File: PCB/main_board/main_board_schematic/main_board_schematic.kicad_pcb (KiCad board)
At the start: 2 copper layers, 257 parts, among them J1 Conn_01x02, J2 Conn_01x02, J3 Conn_01x02, P1 USB_C_Plug_USB2.0, SW1 SW_MEC_5G, SW10 SW_MEC_5G, SW100 SW_MEC_5G, SW101 SW_MEC_5G, SW102 SW_MEC_5G, SW103 SW_MEC_5G, SW104 SW_MEC_5G, SW105 SW_MEC_5G, SW106 SW_MEC_5G, SW107 SW_MEC_5G, SW108 SW_MEC_5G, SW11 SW_MEC_5G, SW12 SW_MEC_5G, SW13 SW_MEC_5G, SW14 SW_MEC_5G, SW15 SW_MEC_5G, SW16 SW_MEC_5G, SW17 SW_MEC_5G, SW18 SW_MEC_5G, SW19 SW_MEC_5G, SW2 SW_MEC_5G, SW20 SW_MEC_5G, SW21 SW_MEC_5G, SW22 SW_MEC_5G, SW23 SW_MEC_5G, SW24 SW_MEC_5G, SW25 SW_MEC_5G, SW26 SW_MEC_5G, SW27 SW_MEC_5G, SW28 SW_MEC_5G, SW29 SW_MEC_5G, SW3 SW_MEC_5G, SW30 SW_MEC_5G, SW31 SW_MEC_5G, SW32 SW_MEC_5G, SW33 SW_MEC_5G, SW34 SW_MEC_5G, SW35 SW_MEC_5G, SW36 SW_MEC_5G, SW37 SW_MEC_5G, SW38 SW_MEC_5G, SW39 SW_MEC_5G, SW4 SW_MEC_5G, SW40 SW_MEC_5G, SW41 SW_MEC_5G, SW42 SW_MEC_5G, SW43 SW_MEC_5G, SW44 SW_MEC_5G, SW45 SW_MEC_5G, SW46 SW_MEC_5G, SW47 SW_MEC_5G, SW48 SW_MEC_5G, SW49 SW_MEC_5G, SW5 SW_MEC_5G, SW50 SW_MEC_5G, SW51 SW_MEC_5G, SW52 SW_MEC_5G, SW53 SW_MEC_5G, SW54 SW_MEC_5G, SW55 SW_MEC_5G, SW56 SW_MEC_5G, SW57 SW_MEC_5G, SW58 SW_MEC_5G, SW59 SW_MEC_5G, SW6 SW_MEC_5G, SW60 SW_MEC_5G, SW61 SW_MEC_5G, SW62 SW_MEC_5G, SW63 SW_MEC_5G, SW64 SW_MEC_5G, SW65 SW_MEC_5G, SW66 SW_MEC_5G, SW67 SW_MEC_5G, SW68 SW_MEC_5G, SW69 SW_MEC_5G, SW7 SW_MEC_5G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

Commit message: Placed large portion of the diodes
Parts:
- removed SW1, SW10, SW104, SW105, SW106, SW108, SW11, SW12, SW13, SW14, SW15, SW16, SW17, SW18, SW19, SW2, SW21, SW22, SW23, SW24, SW25, SW26, SW27, SW28, SW29, SW3, SW31, SW32, SW33, SW34, SW35, SW36, SW37, SW38, SW39, SW4, SW41, SW42, SW43, SW44, SW45, SW46, SW47, SW48, SW49, SW5, SW55, SW56, SW57, SW58, SW59, SW6, SW60, SW61, SW62, SW63, SW64, SW65, SW66, SW67, SW68, SW7, SW70, SW71, SW72, SW73, SW74, SW75, SW76, SW77, SW78, SW79, SW8, SW81, SW82, SW83, SW84, SW85, SW86, SW88, SW89, SW9, SW91, SW92, SW93, SW94, SW96, SW97, SW98, SW99: SW_MEC_5G, Button_Switch_Keyboard:SW_Cherry_MX_1.00u_PCB
- removed SW100, SW87: SW_MEC_5G, Button_Switch_Keyboard:SW_Cherry_MX_2.00u_Vertical_PCB
- removed SW101, SW102, SW103, SW50, SW51, SW52, SW54: SW_MEC_5G, Button_Switch_Keyboard:SW_Cherry_MX_1.25u_PCB
- removed SW107, SW69: SW_MEC_5G, Button_Switch_Keyboard:SW_Cherry_MX_2.00u_PCB
- removed SW20, SW80: SW_MEC_5G, Button_Switch_Keyboard:SW_Cherry_MX_1.50u_PCB
- removed SW30: SW_MEC_5G, Button_Switch_Keyboard:SW_Cherry_MX_1.75u_PCB
- removed SW40, SW90: SW_MEC_5G, Button_Switch_Keyboard:SW_Cherry_MX_2.25u_PCB
- removed SW53: SW_MEC_5G, Button_Switch_Keyboard:SW_Cherry_MX_6.25u_PCB
- removed SW95: SW_MEC_5G, Button_Switch_Keyboard:SW_Cherry_MX_2.75u_PCB
- added MX1: MX_SW_solder, PCM_marbastlib-mx:SW_MX_1u, F.Cu at (28.9, 28.6)
- added MX10: MX_SW_solder, PCM_marbastlib-mx:SW_MX_1u, F.Cu at (28.9, 52.4)
- added MX100: MX_SW_solder, PCM_marbastlib-mx:SW_MX_1u, F.Cu at (438.5, 119.1)
- added MX101: MX_SW_solder, PCM_marbastlib-mx:SW_MX_1.25u, F.Cu at (245.6, 128.6)
- added MX102: MX_SW_solder, PCM_marbastlib-mx:SW_MX_1.25u, F.Cu at (269.4, 128.6)
- added MX103: MX_SW_solder, PCM_marbastlib-mx:SW_MX_1.25u, F.Cu at (293.2, 128.6)
- added MX104: MX_SW_solder, PCM_marbastlib-mx:SW_MX_1u, F.Cu at (319.4, 128.6)
- added MX105: MX_SW_solder, PCM_marbastlib-mx:SW_MX_1u, F.Cu at (338.5, 128.6)
- added MX106: MX_SW_solder, PCM_marbastlib-mx:SW_MX_1u, F.Cu at (357.5, 128.6)
- added MX107: MX_SW_solder, PCM_marbastlib-mx:SW_MX_1u, F.Cu at (390.8, 128.6)
- added MX108: MX_SW_solder, PCM_marbastlib-mx:SW_MX_1u, F.Cu at (419.4, 128.6)
- added MX11: MX_SW_solder, PCM_marbastlib-mx:SW_MX_1u, F.Cu at (47.9, 52.4)
- added MX12: MX_SW_solder, PCM_marbastlib-mx:SW_MX_1u, F.Cu at (67.0, 52.4)
- added MX13: MX_SW_solder, PCM_marbastlib-mx:SW_MX_1u, F.Cu at (86.0, 52.4)
- added MX14: MX_SW_solder, PCM_marbastlib-mx:SW_MX_1u, F.Cu at (105.1, 52.4)
- added MX15: MX_SW_solder, PCM_marbastlib-mx:SW_MX_1u, F.Cu at (124.1, 52.4)
- added MX16: MX_SW_solder, PCM_marbastlib-mx:SW_MX_1u, F.Cu at (143.2, 52.4)
- added MX17: MX_SW_solder, PCM_marbastlib-mx:SW_MX_1u, F.Cu at (162.2, 52.4)
- added MX18: MX_SW_solder, PCM_marbastlib-mx:SW_MX_1u, F.Cu at (181.3, 52.4)
- added MX19: MX_SW_solder, PCM_marbastlib-mx:SW_MX_1u, F.Cu at (200.3, 52.4)
- added MX2: MX_SW_solder, PCM_marbastlib-mx:SW_MX_1u, F.Cu at (67.0, 28.6)
- added MX20: MX_SW_solder, PCM_marbastlib-mx:SW_MX_1.5u, F.Cu at (33.7, 71.4)
- added MX21: MX_SW_solder, PCM_marbastlib-mx:SW_MX_1u, F.Cu at (57.5, 71.4)
- added MX22: MX_SW_solder, PCM_marbastlib-mx:SW_MX_1u, F.Cu at (76.5, 71.4)
- added MX23: MX_SW_solder, PCM_marbastlib-mx:SW_MX_1u, F.Cu at (95.6, 71.4)
- added MX24: MX_SW_solder, PCM_marbastlib-mx:SW_MX_1u, F.Cu at (114.6, 71.4)
- added MX25: MX_SW_solder, PCM_marbastlib-mx:SW_MX_1u, F.Cu at (133.7, 71.4)
- added MX26: MX_SW_solder, PCM_marbastlib-mx:SW_MX_1u, F.Cu at (152.7, 71.4)
- added MX27: MX_SW_solder, PCM_marbastlib-mx:SW_MX_1u, F.Cu at (171.8, 71.4)
- added MX28: MX_SW_solder, PCM_marbastlib-mx:SW_MX_1u, F.Cu at (190.8, 71.4)
- added MX29: MX_SW_solder, PCM_marbastlib-mx:SW_MX_1u, F.Cu at (209.9, 71.4)
- added MX3: MX_SW_solder, PCM_marbastlib-mx:SW_MX_1u, F.Cu at (86.0, 28.6)
- added MX30: MX_SW_solder, PCM_marbastlib-mx:SW_MX_1.75u, F.Cu at (36.0, 90.5)
- added MX31: MX_SW_solder, PCM_marbastlib-mx:SW_MX_1u, F.Cu at (62.2, 90.5)
- added MX32: MX_SW_solder, PCM_marbastlib-mx:SW_MX_1u, F.Cu at (81.3, 90.5)
- added MX33: MX_SW_solder, PCM_marbastlib-mx:SW_MX_1u, F.Cu at (100.3, 90.5)
- added MX34: MX_SW_solder, PCM_marbastlib-mx:SW_MX_1u, F.Cu at (119.4, 90.5)
- added MX35: MX_SW_solder, PCM_marbastlib-mx:SW_MX_1u, F.Cu at (138.4, 90.5)
- added MX36: MX_SW_solder, PCM_marbastlib-mx:SW_MX_1u, F.Cu at (157.5, 90.5)
- added MX37: MX_SW_solder, PCM_marbastlib-mx:SW_MX_1u, F.Cu at (176.5, 90.5)
- added MX38: MX_SW_solder, PCM_marbastlib-mx:SW_MX_1u, F.Cu at (195.6, 90.5)
- added MX39: MX_SW_solder, PCM_marbastlib-mx:SW_MX_1u, F.Cu at (214.6, 90.5)
- added MX4: MX_SW_solder, PCM_marbastlib-mx:SW_MX_1u, F.Cu at (105.1, 28.6)
- added MX40: MX_SW_solder, PCM_marbastlib-mx:SW_MX_1u, F.Cu at (40.8, 109.5)
- added MX41: MX_SW_solder, PCM_marbastlib-mx:SW_MX_1u, F.Cu at (71.8, 109.5)
- added MX42: MX_SW_solder, PCM_marbastlib-mx:SW_MX_1u, F.Cu at (90.8, 109.5)
- added MX43: MX_SW_solder, PCM_marbastlib-mx:SW_MX_1u, F.Cu at (109.9, 109.5)
- added MX44: MX_SW_solder, PCM_marbastlib-mx:SW_MX_1u, F.Cu at (128.9, 109.5)
- added MX45: MX_SW_solder, PCM_marbastlib-mx:SW_MX_1u, F.Cu at (148.0, 109.5)
- added MX46: MX_SW_solder, PCM_marbastlib-mx:SW_MX_1u, F.Cu at (167.0, 109.5)
- added MX47: MX_SW_solder, PCM_marbastlib-mx:SW_MX_1u, F.Cu at (186.1, 109.5)
- added MX48: MX_SW_solder, PCM_marbastlib-mx:SW_MX_1u, F.Cu at (205.1, 109.5)
- added MX49: MX_SW_solder, PCM_marbastlib-mx:SW_MX_1u, F.Cu at (224.2, 109.5)
- added MX5: MX_SW_solder, PCM_marbastlib-mx:SW_MX_1u, F.Cu at (124.1, 28.6)
- added MX50: MX_SW_solder, PCM_marbastlib-mx:SW_MX_1.25u, F.Cu at (31.3, 128.6)
- added MX51: MX_SW_solder, PCM_marbastlib-mx:SW_MX_1.25u, F.Cu at (55.1, 128.6)
- added MX52: MX_SW_solder, PCM_marbastlib-mx:SW_MX_1.25u, F.Cu at (78.9, 128.6)
- added MX53: MX_SW_solder, PCM_marbastlib-mx:SW_MX_1u, F.Cu at (150.3, 128.6)
- added MX54: MX_SW_solder, PCM_marbastlib-mx:SW_MX_1.25u, F.Cu at (221.8, 128.6)
- added MX55: MX_SW_solder, PCM_marbastlib-mx:SW_MX_1u, F.Cu at (238.4, 28.6)
- added MX56: MX_SW_solder, PCM_marbastlib-mx:SW_MX_1u, F.Cu at (257.5, 28.6)
- added MX57: MX_SW_solder, PCM_marbastlib-mx:SW_MX_1u, F.Cu at (276.5, 28.6)
- added MX58: MX_SW_solder, PCM_marbastlib-mx:SW_MX_1u, F.Cu at (295.6, 28.6)
- added MX59: MX_SW_solder, PCM_marbastlib-mx:SW_MX_1u, F.Cu at (319.4, 28.6)
- added MX6: MX_SW_solder, PCM_marbastlib-mx:SW_MX_1u, F.Cu at (152.7, 28.6)
- added MX60: MX_SW_solder, PCM_marbastlib-mx:SW_MX_1u, F.Cu at (338.5, 28.6)
- added MX61: MX_SW_solder, PCM_marbastlib-mx:SW_MX_1u, F.Cu at (357.5, 28.6)
- added MX62: MX_SW_solder, PCM_marbastlib-mx:SW_MX_1u, F.Cu at (381.3, 28.6)
- added MX63: MX_SW_solder, PCM_marbastlib-mx:SW_MX_1u, F.Cu at (400.4, 28.6)
- added MX64: MX_SW_solder, PCM_marbastlib-mx:SW_MX_1u, F.Cu at (419.4, 28.6)
- added MX65: MX_SW_solder, PCM_marbastlib-mx:SW_MX_1u, F.Cu at (438.5, 28.6)
- added MX66: MX_SW_solder, PCM_marbastlib-mx:SW_MX_1u, F.Cu at (219.4, 52.4)
- added MX67: MX_SW_solder, PCM_marbastlib-mx:SW_MX_1u, F.Cu at (238.4, 52.4)
- added MX68: MX_SW_solder, PCM_marbastlib-mx:SW_MX_1u, F.Cu at (257.5, 52.4)
- added MX69: MX_SW_solder, PCM_marbastlib-mx:SW_MX_1u, F.Cu at (286.1, 52.4)
- added MX7: MX_SW_solder, PCM_marbastlib-mx:SW_MX_1u, F.Cu at (171.8, 28.6)
- added MX70: MX_SW_solder, PCM_marbastlib-mx:SW_MX_1u, F.Cu at (319.4, 52.4)
- added MX71: MX_SW_solder, PCM_marbastlib-mx:SW_MX_1u, F.Cu at (338.5, 52.4)
- added MX72: MX_SW_solder, PCM_marbastlib-mx:SW_MX_1u, F.Cu at (357.5, 52.4)
- added MX73: MX_SW_solder, PCM_marbastlib-mx:SW_MX_1u, F.Cu at (381.3, 52.4)
- added MX74: MX_SW_solder, PCM_marbastlib-mx:SW_MX_1u, F.Cu at (400.4, 52.4)
- added MX75: MX_SW_solder, PCM_marbastlib-mx:SW_MX_1u, F.Cu at (419.4, 52.4)
- added MX76: MX_SW_solder, PCM_marbastlib-mx:SW_MX_1u, F.Cu at (438.5, 52.4)
- added MX77: MX_SW_solder, PCM_marbastlib-mx:SW_MX_1u, F.Cu at (228.9, 71.4)
- added MX78: MX_SW_solder, PCM_marbastlib-mx:SW_MX_1u, F.Cu at (248.0, 71.4)
- added MX79: MX_SW_solder, PCM_marbastlib-mx:SW_MX_1u, F.Cu at (267.0, 71.4)
- added MX8: MX_SW_solder, PCM_marbastlib-mx:SW_MX_1u, F.Cu at (190.8, 28.6)
- added MX80: MX_SW_solder, PCM_marbastlib-mx:SW_MX_1.5u, F.Cu at (290.8, 71.4)
- added MX81: MX_SW_solder, PCM_marbastlib-mx:SW_MX_1u, F.Cu at (319.4, 71.4)
- added MX82: MX_SW_solder, PCM_marbastlib-mx:SW_MX_1u, F.Cu at (338.5, 71.4)
- added MX83: MX_SW_solder, PCM_marbastlib-mx:SW_MX_1u, F.Cu at (357.5, 71.4)
- added MX84: MX_SW_solder, PCM_marbastlib-mx:SW_MX_1u, F.Cu at (381.3, 71.4)
- added MX85: MX_SW_solder, PCM_marbastlib-mx:SW_MX_1u, F.Cu at (400.4, 71.4)
- added MX86: MX_SW_solder, PCM_marbastlib-mx:SW_MX_1u, F.Cu at (419.4, 71.4)
- added MX87: MX_SW_solder, PCM_marbastlib-mx:SW_MX_1u, F.Cu at (438.5, 81.0)
- added MX88: MX_SW_solder, PCM_marbastlib-mx:SW_MX_1u, F.Cu at (233.7, 90.5)
- added MX89: MX_SW_solder, PCM_marbastlib-mx:SW_MX_1u, F.Cu at (252.7, 90.5)
- added MX9: MX_SW_solder, PCM_marbastlib-mx:SW_MX_1u, F.Cu at (209.9, 28.6)
- added MX90: MX_SW_solder, PCM_marbastlib-mx:SW_MX_1u, F.Cu at (283.7, 90.5)
- added MX91: MX_SW_solder, PCM_marbastlib-mx:SW_MX_1u, F.Cu at (381.3, 90.5)
- added MX92: MX_SW_solder, PCM_marbastlib-mx:SW_MX_1u, F.Cu at (400.4, 90.5)
- added MX93: MX_SW_solder, PCM_marbastlib-mx:SW_MX_1u, F.Cu at (419.4, 90.5)
- added MX94: MX_SW_solder, PCM_marbastlib-mx:SW_MX_1u, F.Cu at (243.2, 109.5)
- added MX95: MX_SW_solder, PCM_marbastlib-mx:SW_MX_1u, F.Cu at (278.9, 109.5)
- added MX96: MX_SW_solder, PCM_marbastlib-mx:SW_MX_1u, F.Cu at (338.5, 109.5)
- added MX97: MX_SW_solder, PCM_marbastlib-mx:SW_MX_1u, F.Cu at (381.3, 109.5)
- added MX98: MX_SW_solder, PCM_marbastlib-mx:SW_MX_1u, F.Cu at (400.4, 109.5)
- added MX99: MX_SW_solder, PCM_marbastlib-mx:SW_MX_1u, F.Cu at (419.4, 109.5)
- D1, D10, D101, D102, D103, D11, D12, D13, D14, D15, D16, D17, D18, D19, D2, D20, D21, D22, D23, D24, D25, D26, D27, D28, D29, D3, D30, D31, D32, D33, D34, D35, D36, D37, D38, D39, D4, D40, D41, D42, D43, D44, D45, D46, D47, D48, D49, D5, D50, D51, D52, D53, D54, D55, D56, D57, D58, D6, D66, D67, D68, D69, D7, D77, D78, D79, D8, D80, D88, D89, D9, D90, D94, D95: moved to B.Cu
- P1: footprint Connector_USB:USB_C_Receptacle_GCT_USB4135-GF-A_6P_TopMnt_Horizontal -> Connector_USB:USB_C_Receptacle_G-Switch_GT-USB-7010ASV
- S2, S5: footprint PCM_marbastlib-mx:STAB_MX_2u -> PCM_marbastlib-mx:STAB_MX_P_2.25u
- S3, S4, S7, S8: footprint PCM_marbastlib-mx:STAB_MX_2u -> PCM_marbastlib-mx:STAB_MX_P_2u
- S6: footprint PCM_marbastlib-mx:STAB_MX_2u -> PCM_marbastlib-mx:STAB_MX_P_2.75u
- moved S2 524.5 mm to (40.8, 109.5), turned to 180 degrees
- moved D1 484.3 mm to (21.4, 25.8), turned to 180 degrees
- moved D10 483.5 mm to (21.4, 49.6), turned to 180 degrees
- moved D20 472.6 mm to (26.2, 68.7), turned to 180 degrees
- moved D11 467.5 mm to (40.5, 49.6), turned to 180 degrees
- moved D30 465.0 mm to (28.6, 87.7), turned to 180 degrees
- moved D50 462.4 mm to (23.8, 125.8), turned to 180 degrees
- moved D40 456.2 mm to (33.3, 106.8), turned to 180 degrees
- moved D21 451.8 mm to (50.0, 68.7), turned to 180 degrees
- moved D12 451.6 mm to (59.6, 49.6), turned to 180 degrees
- moved D2 451.3 mm to (59.5, 25.8), turned to 180 degrees
- moved D31 441.4 mm to (54.8, 87.7), turned to 180 degrees
- moved D51 439.8 mm to (47.7, 125.8), turned to 180 degrees
- moved D3 435.8 mm to (78.6, 25.8), turned to 180 degrees
- moved D22 435.5 mm to (69.2, 68.7), turned to 180 degrees
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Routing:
- net /IN9: track 0.00 -> 233.8 mm
- net /OUT7: track 0.00 -> 220.4 mm
- net /IN8: track 0.00 -> 215.7 mm
- net /OUT8: track 0.00 -> 213.5 mm
- net /IN6: track 0.00 -> 211.7 mm
- net /OUT6: track 0.00 -> 200.0 mm
- net /OUT10: track 0.00 -> 199.2 mm
- net /OUT9: track 0.00 -> 191.2 mm
- net /OUT5: track 0.00 -> 190.5 mm
- net /OUT4: track 0.00 -> 183.4 mm
- net /OUT0: track 0.00 -> 181.0 mm
- net /OUT3: track 0.00 -> 178.6 mm
- net /OUT2: track 0.00 -> 176.2 mm
- net /OUT11: track 0.00 -> 173.8 mm
- net /OUT1: track 0.00 -> 171.4 mm
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
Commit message: Added all diodes to key matrix
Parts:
- D100, D104, D105, D106, D107, D108, D59, D60, D61, D62, D63, D64, D65, D70, D71, D72, D73, D74, D75, D76, D81, D82, D83, D84, D85, D86, D87, D91, D92, D93, D96, D97, D98, D99: moved to B.Cu
- moved D59 443.1 mm to (311.9, 25.8), turned to 180 degrees
- moved D70 435.8 mm to (311.9, 49.6), turned to 180 degrees
- moved D81 431.5 mm to (312.0, 68.7), turned to 180 degrees
- moved D104 428.4 mm to (312.0, 125.8), turned to 180 degrees
- moved D60 427.1 mm to (331.0, 25.8), turned to 180 degrees
- moved D71 419.3 mm to (330.9, 49.6), turned to 180 degrees
- moved D82 414.5 mm to (331.0, 68.7), turned to 180 degrees
- moved D105 410.3 mm to (331.0, 125.8), turned to 180 degrees
- moved D96 407.5 mm to (331.0, 106.8), turned to 180 degrees
- moved D72 402.8 mm to (350.0, 49.6), turned to 180 degrees
- moved D61 401.5 mm to (350.0, 25.8), turned to 180 degrees
- moved D83 397.6 mm to (350.0, 68.7), turned to 180 degrees
- moved D106 392.2 mm to (350.0, 125.8), turned to 180 degrees
- moved D62 381.0 mm to (373.9, 25.8), turned to 180 degrees
- moved D84 376.5 mm to (373.9, 68.7), turned to 180 degrees
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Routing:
- net /IN2: track 115.0 -> 219.0 mm
- net /IN4: track 90.9 -> 191.0 mm
- net /IN5: track 110.9 -> 210.9 mm
- net /IN3: track 91.0 -> 191.0 mm
- net /IN10: track 0.00 -> 96.7 mm
- net /IN1: track 96.7 -> 177.7 mm
- net Net-(D71-K): track 0.00 -> 3.14 mm
- net Net-(D65-K): track 0.00 -> 3.05 mm
- net Net-(D59-K): track 0.00 -> 3.05 mm
- net Net-(D87-K): track 0.00 -> 3.05 mm
- net Net-(D70-K): track 0.00 -> 3.05 mm
- net Net-(D107-K): track 0.00 -> 3.05 mm
- net Net-(D100-K): track 0.00 -> 3.05 mm
- net Net-(D92-K): track 0.00 -> 3.05 mm
- net Net-(D91-K): track 0.00 -> 3.05 mm
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
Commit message: placed the rp2040 inside the board
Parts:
- C1, C10, C11, C12, C13, C14, C17, C2, C3, C4, C5, C6, C7, C8, C9, J2, R1, R6, R7, U2, U3, Y1: moved to B.Cu
- moved U3 481.7 mm to (327.3, 86.4), turned to 180 degrees
- moved U2 467.2 mm to (315.2, 94.7), turned to 180 degrees
- moved C13 430.6 mm to (310.3, 87.2), turned to 90 degrees
- moved C12 428.3 mm to (311.9, 87.2), turned to 90 degrees
- moved J2 427.5 mm to (329.0, 13.7), turned to 90 degrees
- moved C9 427.4 mm to (309.2, 90.2), turned to 180 degrees
- moved C14 426.9 mm to (318.5, 114.6), turned to 90 degrees
- moved C10 426.4 mm to (309.2, 95.8), turned to 180 degrees
- moved C3 425.6 mm to (308.9, 87.2), turned to 90 degrees
- moved C17 422.8 mm to (321.3, 83.4), turned to 90 degrees
- moved C4 420.4 mm to (315.3, 87.2), turned to 90 degrees
- moved Y1 420.4 mm to (313.7, 110.2)
- moved C8 420.2 mm to (316.9, 87.2), turned to 90 degrees
- moved R6 419.4 mm to (328.5, 82.1)
- moved C7 419.2 mm to (314.3, 101.4), turned to -90 degrees
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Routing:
- net /IN4: track 191.0 -> 277.9 mm
- net /IN3: track 191.0 -> 227.2 mm
- net /OUT10: track 199.2 -> 217.0 mm
- net /IN5: track 210.9 -> 219.0 mm
- net Net-(D40-K): track 3.32 -> 0.27 mm
- net +3V3: track 0.00 -> 0.70 mm

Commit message: Placed and connected all components
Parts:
- removed C3: 100n, Capacitor_SMD:C_0603_1608Metric
- C15, C16, J3, P1, R2, R3, R4, R5, R8, U1: moved to B.Cu
- moved P1 496.4 mm to (305.5, 26.2)
- moved U1 477.1 mm to (303.6, 100.0), turned to -90 degrees
- moved R4 461.1 mm to (303.5, 36.7), turned to -90 degrees
- moved R5 454.6 mm to (307.8, 36.7), turned to -90 degrees
- moved J3 452.2 mm to (296.2, 29.6), turned to 90 degrees
- moved C15 436.3 mm to (302.1, 93.3), turned to 180 degrees
- moved R8 434.0 mm to (306.1, 109.0), turned to 90 degrees
- moved C16 433.7 mm to (301.6, 106.8), turned to 180 degrees
- moved R3 425.2 mm to (315.8, 99.4), turned to 90 degrees
- moved R2 423.0 mm to (317.3, 99.4), turned to -90 degrees
- moved J1 256.6 mm to (461.4, 123.2), turned to -90 degrees
- moved J2 19.4 mm to (317.8, 29.6)
- moved R7 18.7 mm to (336.6, 99.5)
- moved R6 16.3 mm to (335.0, 97.1), turned to -90 degrees
- moved C17 14.9 mm to (332.4, 93.3)
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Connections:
- J1 pad 2: /SWDCLK -> /SWCLK
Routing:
- net /IN0: track 108.9 -> 613.1 mm
- net /IN1: track 177.7 -> 564.1 mm
- net /IN2: track 219.0 -> 542.0 mm
- net /IN5: track 219.0 -> 495.1 mm, vias 0 -> 4
- net /IN3: track 227.2 -> 493.2 mm
- net /OUT6: track 200.0 -> 431.3 mm, vias 0 -> 3
- net /IN4: track 277.9 -> 502.5 mm
- net /IN7: track 149.6 -> 360.9 mm
- net /OUT7: track 220.4 -> 398.6 mm, vias 0 -> 3
- net /IN6: track 211.7 -> 384.3 mm
- net /OUT8: track 213.5 -> 358.9 mm, vias 0 -> 1
- net /IN8: track 215.7 -> 338.5 mm
- net /IN9: track 233.8 -> 343.6 mm
- net /RUN: track 0.00 -> 102.7 mm, vias 0 -> 2
- net /USB_D+: track 0.00 -> 78.2 mm, vias 0 -> 2
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- added copper zone on B.Cu, net +3V3
- added copper zone on F.Cu, net GND

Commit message: Connected matrix to the rp2040
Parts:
- J1: footprint Connector_PinHeader_2.54mm:PinHeader_1x02_P2.54mm_Horizontal -> Connector_PinHeader_2.54mm:PinHeader_1x02_P2.54mm_Vertical; moved to B.Cu
- J2, J3: footprint Connector_PinHeader_2.54mm:PinHeader_1x02_P2.54mm_Horizontal -> Connector_PinHeader_2.54mm:PinHeader_1x02_P2.54mm_Vertical
- moved J1 146.0 mm to (315.4, 120.7), turned to 180 degrees
- moved R5 12.7 mm to (317.3, 45.1)
- moved R4 12.1 mm to (312.3, 45.0)
- moved P1 10.2 mm to (313.6, 32.4)
- moved D59 9.71 mm to (320.3, 37.9)
- moved C17 9.34 mm to (341.7, 93.2)
- moved C4 9.34 mm to (321.2, 101.4)
- moved C6 9.34 mm to (333.5, 107.6)
- moved C9 9.34 mm to (321.2, 102.9)
- moved D108 9.34 mm to (419.9, 137.3)
- moved D57 9.34 mm to (277.1, 37.3)
- moved D64 9.34 mm to (419.9, 37.3)
- moved D75 9.34 mm to (419.9, 61.1)
- moved D86 9.34 mm to (420.0, 80.2)
- moved D93 9.34 mm to (419.9, 99.2)
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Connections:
- D1 pad 2: /IN0 -> /GPIO12
- D10 pad 2: /IN0 -> /GPIO12
- D100 pad 2: /IN10 -> /GPIO11
- D101 pad 2: /IN9 -> /GPIO18
- D102 pad 2: /IN8 -> /GPIO19
- D103 pad 2: /IN6 -> /GPIO21
- D104 pad 2: /IN5 -> /GPIO17
- D105 pad 2: /IN4 -> /GPIO16
- D106 pad 2: /IN3 -> /GPIO15
- D107 pad 2: /IN2 -> /GPIO14
- D108 pad 2: /IN0 -> /GPIO12
- D11 pad 2: /IN1 -> /GPIO13
- D12 pad 2: /IN2 -> /GPIO14
- D13 pad 2: /IN3 -> /GPIO15
- D14 pad 2: /IN4 -> /GPIO16
- D15 pad 2: /IN5 -> /GPIO17
- D16 pad 2: /IN6 -> /GPIO21
- D17 pad 2: /IN7 -> /GPIO20
- D18 pad 2: /IN8 -> /GPIO19
- D19 pad 2: /IN9 -> /GPIO18
- D2 pad 2: /IN2 -> /GPIO14
- D20 pad 2: /IN0 -> /GPIO12
- D21 pad 2: /IN1 -> /GPIO13
- D22 pad 2: /IN2 -> /GPIO14
- D23 pad 2: /IN3 -> /GPIO15
- D24 pad 2: /IN4 -> /GPIO16
- D25 pad 2: /IN5 -> /GPIO17
- D26 pad 2: /IN6 -> /GPIO21
- D27 pad 2: /IN7 -> /GPIO20
- D28 pad 2: /IN8 -> /GPIO19
- D29 pad 2: /IN9 -> /GPIO18
- D3 pad 2: /IN3 -> /GPIO15
- D30 pad 2: /IN0 -> /GPIO12
- D31 pad 2: /IN1 -> /GPIO13
- D32 pad 2: /IN2 -> /GPIO14
- D33 pad 2: /IN3 -> /GPIO15
- D34 pad 2: /IN4 -> /GPIO16
- D35 pad 2: /IN5 -> /GPIO17
- D36 pad 2: /IN6 -> /GPIO21
- D37 pad 2: /IN7 -> /GPIO20
- D38 pad 2: /IN8 -> /GPIO19
- D39 pad 2: /IN9 -> /GPIO18
- D4 pad 2: /IN4 -> /GPIO16
- D40 pad 2: /IN0 -> /GPIO12
- D41 pad 2: /IN1 -> /GPIO13
- D42 pad 2: /IN2 -> /GPIO14
- D43 pad 2: /IN3 -> /GPIO15
- D44 pad 2: /IN4 -> /GPIO16
- D45 pad 2: /IN5 -> /GPIO17
- D46 pad 2: /IN6 -> /GPIO21
- D47 pad 2: /IN7 -> /GPIO20
- D48 pad 2: /IN8 -> /GPIO19
- D49 pad 2: /IN9 -> /GPIO18
- D5 pad 2: /IN5 -> /GPIO17
- D50 pad 2: /IN0 -> /GPIO12
- D51 pad 2: /IN1 -> /GPIO13
- D52 pad 2: /IN2 -> /GPIO14
- D53 pad 2: /IN5 -> /GPIO17
- D54 pad 2: /IN9 -> /GPIO18
- D55 pad 2: /IN9 -> /GPIO18
- D56 pad 2: /IN8 -> /GPIO19
- D57 pad 2: /IN7 -> /GPIO20
- D58 pad 2: /IN6 -> /GPIO21
- D59 pad 2: /IN5 -> /GPIO17
- D6 pad 2: /IN6 -> /GPIO21
- D60 pad 2: /IN4 -> /GPIO16
- D61 pad 2: /IN3 -> /GPIO15
- D62 pad 2: /IN2 -> /GPIO14
- D63 pad 2: /IN1 -> /GPIO13
- D64 pad 2: /IN0 -> /GPIO12
- D65 pad 2: /IN10 -> /GPIO11
- D66 pad 2: /IN9 -> /GPIO18
- D67 pad 2: /IN8 -> /GPIO19
- D68 pad 2: /IN7 -> /GPIO20
- D69 pad 2: /IN6 -> /GPIO21
- D7 pad 2: /IN7 -> /GPIO20
- D70 pad 2: /IN5 -> /GPIO17
- D71 pad 2: /IN4 -> /GPIO16
- D72 pad 2: /IN3 -> /GPIO15
- D73 pad 2: /IN2 -> /GPIO14
- D74 pad 2: /IN1 -> /GPIO13
- D75 pad 2: /IN0 -> /GPIO12
- D76 pad 2: /IN10 -> /GPIO11
- D77 pad 2: /IN9 -> /GPIO18
- D78 pad 2: /IN8 -> /GPIO19
- D79 pad 2: /IN7 -> /GPIO20
- D8 pad 2: /IN8 -> /GPIO19
- D80 pad 2: /IN6 -> /GPIO21
- D81 pad 2: /IN5 -> /GPIO17
- D82 pad 2: /IN4 -> /GPIO16
- D83 pad 2: /IN3 -> /GPIO15
- D84 pad 2: /IN2 -> /GPIO14
- D85 pad 2: /IN1 -> /GPIO13
- D86 pad 2: /IN0 -> /GPIO12
- D87 pad 2: /IN10 -> /GPIO11
- D88 pad 2: /IN9 -> /GPIO18
- D89 pad 2: /IN8 -> /GPIO19
- D9 pad 2: /IN9 -> /GPIO18
- D90 pad 2: /IN6 -> /GPIO21
- D91 pad 2: /IN2 -> /GPIO14
- D92 pad 2: /IN1 -> /GPIO13
- D93 pad 2: /IN0 -> /GPIO12
- D94 pad 2: /IN9 -> /GPIO18
- D95 pad 2: /IN6 -> /GPIO21
- D96 pad 2: /IN4 -> /GPIO16
- D97 pad 2: /IN2 -> /GPIO14
- D98 pad 2: /IN1 -> /GPIO13
- D99 pad 2: /IN0 -> /GPIO12
- MX1 pad 2: /OUT0 -> /GPIO28
- MX10 pad 2: /OUT1 -> /GPIO27
- MX100 pad 2: /OUT10 -> /GPIO6
- MX101 pad 2: /OUT11 -> /GPIO7
- MX102 pad 2: /OUT11 -> /GPIO7
- MX103 pad 2: /OUT11 -> /GPIO7
- MX104 pad 2: /OUT11 -> /GPIO7
- MX105 pad 2: /OUT11 -> /GPIO7
- MX106 pad 2: /OUT11 -> /GPIO7
- MX107 pad 2: /OUT11 -> /GPIO7
- MX108 pad 2: /OUT11 -> /GPIO7
- MX11 pad 2: /OUT1 -> /GPIO27
- MX12 pad 2: /OUT1 -> /GPIO27
- MX13 pad 2: /OUT1 -> /GPIO27
- MX14 pad 2: /OUT1 -> /GPIO27
- MX15 pad 2: /OUT1 -> /GPIO27
- MX16 pad 2: /OUT1 -> /GPIO27
- MX17 pad 2: /OUT1 -> /GPIO27
- MX18 pad 2: /OUT1 -> /GPIO27
- MX19 pad 2: /OUT1 -> /GPIO27
- MX2 pad 2: /OUT0 -> /GPIO28
- MX20 pad 2: /OUT2 -> /GPIO26
- MX21 pad 2: /OUT2 -> /GPIO26
- MX22 pad 2: /OUT2 -> /GPIO26
- MX23 pad 2: /OUT2 -> /GPIO26
- MX24 pad 2: /OUT2 -> /GPIO26
- MX25 pad 2: /OUT2 -> /GPIO26
- MX26 pad 2: /OUT2 -> /GPIO26
- MX27 pad 2: /OUT2 -> /GPIO26
- MX28 pad 2: /OUT2 -> /GPIO26
- MX29 pad 2: /OUT2 -> /GPIO26
- MX3 pad 2: /OUT0 -> /GPIO28
- MX30 pad 2: /OUT3 -> /GPIO24
- MX31 pad 2: /OUT3 -> /GPIO24
- MX32 pad 2: /OUT3 -> /GPIO24
- MX33 pad 2: /OUT3 -> /GPIO24
- MX34 pad 2: /OUT3 -> /GPIO24
- MX35 pad 2: /OUT3 -> /GPIO24
- MX36 pad 2: /OUT3 -> /GPIO24
- MX37 pad 2: /OUT3 -> /GPIO24
- MX38 pad 2: /OUT3 -> /GPIO24
- MX39 pad 2: /OUT3 -> /GPIO24
- MX4 pad 2: /OUT0 -> /GPIO28
- MX40 pad 2: /OUT4 -> /GPIO23
- MX41 pad 2: /OUT4 -> /GPIO23
- MX42 pad 2: /OUT4 -> /GPIO23
- MX43 pad 2: /OUT4 -> /GPIO23
- MX44 pad 2: /OUT4 -> /GPIO23
- MX45 pad 2: /OUT4 -> /GPIO23
- MX46 pad 2: /OUT4 -> /GPIO23
- MX47 pad 2: /OUT4 -> /GPIO23
- MX48 pad 2: /OUT4 -> /GPIO23
- MX49 pad 2: /OUT4 -> /GPIO23
- MX5 pad 2: /OUT0 -> /GPIO28
- MX50 pad 2: /OUT5 -> /GPIO22
- MX51 pad 2: /OUT5 -> /GPIO22
- MX52 pad 2: /OUT5 -> /GPIO22
- MX53 pad 2: /OUT5 -> /GPIO22
- MX54 pad 2: /OUT5 -> /GPIO22
- MX55 pad 2: /OUT6 -> /GPIO2
- MX56 pad 2: /OUT6 -> /GPIO2
- MX57 pad 2: /OUT6 -> /GPIO2
- MX58 pad 2: /OUT6 -> /GPIO2
- MX59 pad 2: /OUT6 -> /GPIO2
- MX6 pad 2: /OUT0 -> /GPIO28
- MX60 pad 2: /OUT6 -> /GPIO2
- MX61 pad 2: /OUT6 -> /GPIO2
- MX62 pad 2: /OUT6 -> /GPIO2
- MX63 pad 2: /OUT6 -> /GPIO2
- MX64 pad 2: /OUT6 -> /GPIO2
- MX65 pad 2: /OUT6 -> /GPIO2
- MX66 pad 2: /OUT7 -> /GPIO3
- MX67 pad 2: /OUT7 -> /GPIO3
- MX68 pad 2: /OUT7 -> /GPIO3
- MX69 pad 2: /OUT7 -> /GPIO3
- MX7 pad 2: /OUT0 -> /GPIO28
- MX70 pad 2: /OUT7 -> /GPIO3
- MX71 pad 2: /OUT7 -> /GPIO3
- MX72 pad 2: /OUT7 -> /GPIO3
- MX73 pad 2: /OUT7 -> /GPIO3
- MX74 pad 2: /OUT7 -> /GPIO3
- MX75 pad 2: /OUT7 -> /GPIO3
- MX76 pad 2: /OUT7 -> /GPIO3
- MX77 pad 2: /OUT8 -> /GPIO4
- MX78 pad 2: /OUT8 -> /GPIO4
- MX79 pad 2: /OUT8 -> /GPIO4
- MX8 pad 2: /OUT0 -> /GPIO28
- MX80 pad 2: /OUT8 -> /GPIO4
- MX81 pad 2: /OUT8 -> /GPIO4
- MX82 pad 2: /OUT8 -> /GPIO4
- MX83 pad 2: /OUT8 -> /GPIO4
- MX84 pad 2: /OUT8 -> /GPIO4
- MX85 pad 2: /OUT8 -> /GPIO4
- MX86 pad 2: /OUT8 -> /GPIO4
- MX87 pad 2: /OUT8 -> /GPIO4
- MX88 pad 2: /OUT9 -> /GPIO5
- MX89 pad 2: /OUT9 -> /GPIO5
- MX9 pad 2: /OUT0 -> /GPIO28
- MX90 pad 2: /OUT9 -> /GPIO5
- MX91 pad 2: /OUT9 -> /GPIO5
- MX92 pad 2: /OUT9 -> /GPIO5
- MX93 pad 2: /OUT9 -> /GPIO5
- MX94 pad 2: /OUT10 -> /GPIO6
- MX95 pad 2: /OUT10 -> /GPIO6
- MX96 pad 2: /OUT10 -> /GPIO6
- MX97 pad 2: /OUT10 -> /GPIO6
- MX98 pad 2: /OUT10 -> /GPIO6
- MX99 pad 2: /OUT10 -> /GPIO6
- U2 pad 11: /GPIO8 -> GND
- U2 pad 12: /GPIO9 -> GND
- U2 pad 13: /GPIO10 -> GND
- U2 pad 2: /GPIO0 -> GND
- U2 pad 3: /GPIO1 -> GND
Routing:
- net /GPIO12: track 0.99 -> 674.0 mm, vias 0 -> 4
- net /GPIO13: track 1.03 -> 626.6 mm, vias 0 -> 4
- net /IN0: track 613.1 -> 0.00 mm
- net /GPIO14: track 1.49 -> 602.7 mm, vias 0 -> 4
- net /IN1: track 564.1 -> 0.00 mm
- net /GPIO15: track 1.87 -> 552.4 mm, vias 0 -> 4
- net /GPIO16: track 2.05 -> 551.4 mm
- net /IN2: track 542.0 -> 0.00 mm
- net /GPIO17: track 1.64 -> 526.6 mm, vias 0 -> 4
- net /IN4: track 502.5 -> 0.00 mm
- net /IN5: track 495.1 -> 0.00 mm, vias 4 -> 0
- net /IN3: track 493.2 -> 0.00 mm
- net /GPIO2: track 11.0 -> 478.9 mm, vias 0 -> 3
- net /GPIO3: track 10.2 -> 447.2 mm, vias 0 -> 3
- net /OUT6: track 431.3 -> 0.00 mm, vias 3 -> 0
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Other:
- board outline added: 433.7 x 124.3 mm

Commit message: Moved usb-c connector and added labels
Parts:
- moved P1 1.06 mm to (313.6, 31.3)
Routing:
- net VBUS: track 81.3 -> 79.7 mm
- net /USB_D-: track 68.6 -> 69.7 mm
- net /USB_D+: track 72.2 -> 73.0 mm
- net Net-(P1-VCONN): track 9.33 -> 10.1 mm
- net Net-(P1-CC): track 8.14 -> 8.92 mm
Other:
- board size 433.7 x 124.3 mm -> 434.6 x 125.1 mm

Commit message: Added a led connected to pin25
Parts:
- added D109: LED, LED_SMD:LED_0603_1608Metric, B.Cu at (317.2, 117.2)
- added R9: 300, Resistor_SMD:R_0603_1608Metric, B.Cu at (318.8, 117.2)
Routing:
- net /GPIO25: track 15.5 -> 23.2 mm, vias 1 -> 2
- net /RUN: track 104.3 -> 108.4 mm
- net Net-(D109-K): track 0.00 -> 1.63 mm
- net GND: track 56.1 -> 57.6 mm, vias 33 -> 34

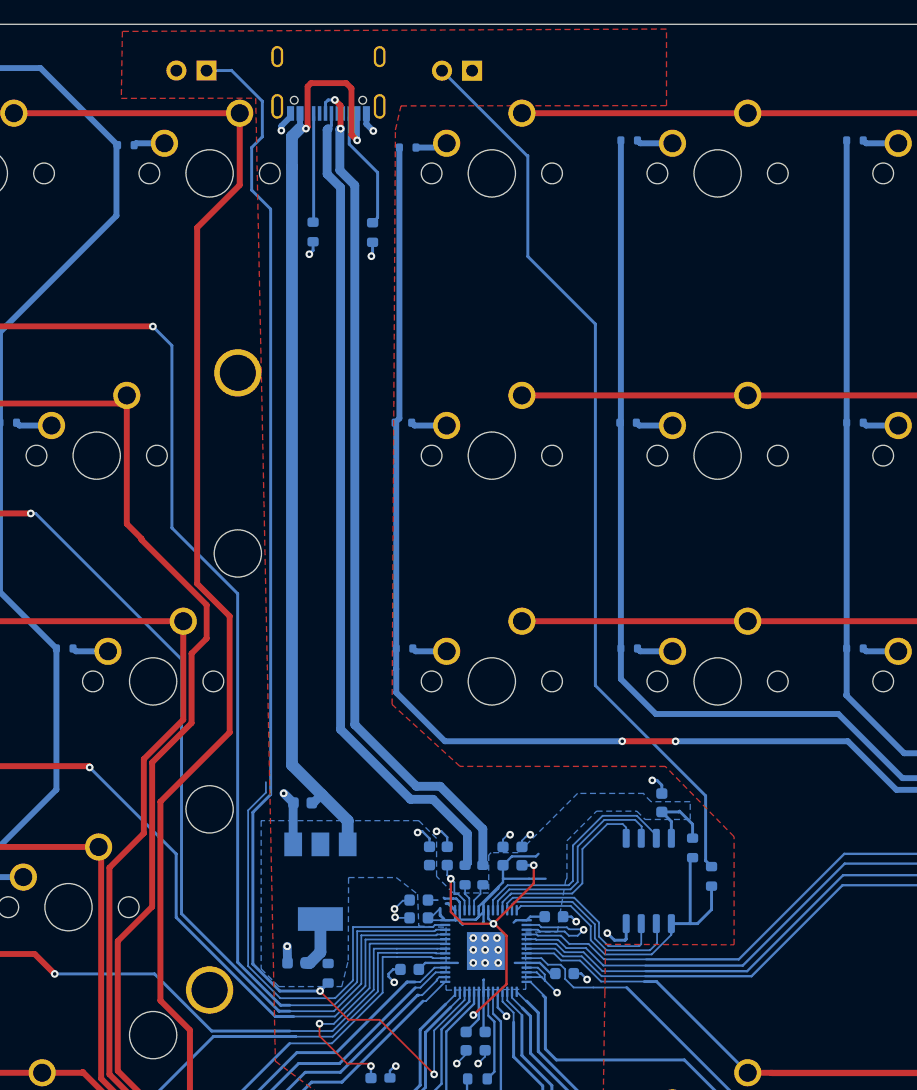
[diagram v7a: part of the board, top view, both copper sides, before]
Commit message: Exposed pins and power rails
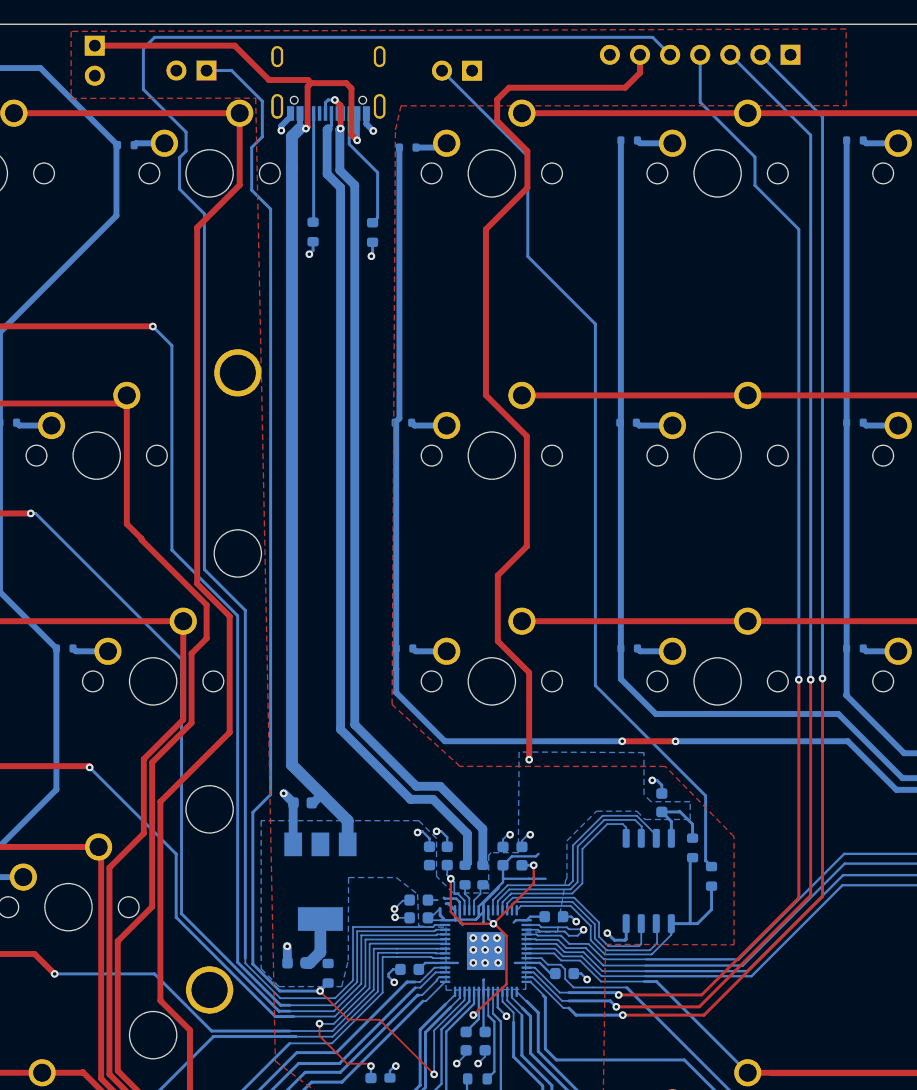
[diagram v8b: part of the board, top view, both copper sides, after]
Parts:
- added J4: Conn_01x07, Connector_PinSocket_2.54mm:PinSocket_1x07_P2.54mm_Vertical, B.Cu at (352.6, 30.1)
- added J5: Conn_01x02, Connector_PinSocket_2.54mm:PinSocket_1x02_P2.54mm_Vertical, B.Cu at (293.9, 29.3)
- R9: value 300 -> 100
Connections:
- U2 pad 11: GND -> /GPIO8
- U2 pad 12: GND -> /GPIO9
- U2 pad 13: GND -> /GPIO10
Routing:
- net /GPIO29: track 39.1 -> 149.9 mm
- net /GPIO10: track 0.00 -> 103.6 mm, vias 0 -> 2
- net /GPIO9: track 0.00 -> 102.8 mm, vias 0 -> 2
- net /GPIO8: track 0.00 -> 102.2 mm, vias 0 -> 2
- net +3V3: track 56.5 -> 132.7 mm, vias 0 -> 1
- net VBUS: track 79.7 -> 99.3 mm
- net GND: track 57.6 -> 50.7 mm, vias 34 -> 33
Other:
- board text added: "+3V3"
- board text added: "08"
- board text added: "09"
- board text added: "10"
- board text added: "29"
- board text added: "GND"
- board text added: "RESET"
- board text added: "USB-BOOT"
- board text added: "VBUS"
